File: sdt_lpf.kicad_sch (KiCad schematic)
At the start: 54 parts, among them J1 5-1814832-1, J2 5-1814832-1, J3 Conn_02x05_Odd_Even, U1 MASWSS0179, U10 MASWSS0179, U11 74LVC14AS14-13, U2 MASWSS0179, U3 MASWSS0179, U4 MASWSS0179, U5 MASWSS0179, U6 MASWSS0179, U7 MASWSS0179, U8 MASWSS0179, U9 MASWSS0179

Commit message: Commit before SSD update.
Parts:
- C1: footprint (none) -> 74LVC14:SO14_DIO
- C10, C11, C12, C13, C14, C15, C16, C17, C18, C19, C2, C20, C21, C22, C23, C24, C25, C3, C4, C5, C6, C7, C8, C9: footprint (none) -> Capacitor_SMD:C_1206_3216Metric
- R1: footprint (none) -> Resistor_SMD:R_1206_3216Metric
- U11: footprint SO14_DIO -> 74LVC14:SO14_DIO
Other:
- note added: "0.32 uH"
- note added: "0.4 uH"
- note added: "0.58u"
- note added: "1 db ripple Chebyshev 5th order coefficients 2.1349 1.0911 3.0009 1.0911 2.1349"
- note added: "1.09 uH"
- note added: "1.74 uH"
- note added: "1195 pF"
- note added: "1360 pF"
- note added: "15 MHz cut-off"
- note added: "1911 pF"
- note added: "22 MHz cut-off"
- note added: "227 pF"
- note added: "30 MHz cut-off"
- note added: "309 pF"
- note added: "319 pF"
- note added: "434 pF"
- note added: "453p"
- note added: "5 MHz cut-off"
- note added: "637p"
- note added: "8 MHz cut-off"
- note added: "850 pF"
- moved on the sheet: C1, C10, C11, C12, C13, C14, C15, C16, C17, C18, C19, C2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

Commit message: Released to PCBWay June 23.
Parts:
- removed D1, D2, D3, D4: 1N4148W, Diode_SMD:D_SOD-123, symbol Diode:1N4148W
- removed R1: R_US, Resistor_SMD:R_1206_3216Metric, symbol Device:R_US
- removed U11: 74LVC14AS14-13, 74LVC14:SO14_DIO, symbol 74LVC14AS14-13:74LVC14AS14-13
- added C26, C27, C28, C29, C30: 0.01u, Capacitor_SMD:C_1206_3216Metric, symbol Device:C
- added C31, C32, C33, C34, C35, C36: 0.1u, Capacitor_SMD:C_1206_3216Metric, symbol Device:C
- added H1, H2, H3, H4: MountingHole, MountingHole:MountingHole_3.2mm_M3, symbol Mechanical:MountingHole
- added J3: 22-23-2021, digikey-footprints:PinHeader_1x2_P2.54mm_Drill1.02mm, symbol dk_Rectangular-Connectors-Headers-Male-Pins:22-23-2021
- added U12: SN74HCS21, 74LVC14:SO14_DIO, symbol dk_Logic-Buffers-Drivers-Receivers-Transceivers:SN74HCS21
- C1: renamed from C16; value C -> 0.01u
- C2: renamed from C17; value C -> 0.01u
- C21: renamed from C25; value C -> 0.01u
- C22: renamed from C24; value C -> 0.01u
- C23: value C -> 0.01u
- C24: renamed from C22; value C -> 0.01u
- C25: renamed from C21; value C -> 0.01u
- C3: renamed from C18; value C -> 0.01u
- C4: renamed from C19; value C -> 0.01u
- C5: renamed from C20; value C -> 0.01u
- C7: renamed from C1; footprint 74LVC14:SO14_DIO -> Capacitor_SMD:C_1206_3216Metric
- J4: renamed from J3; footprint (none) -> Connector_PinHeader_2.54mm:PinHeader_2x05_P2.54mm_Vertical
- L1: renamed from L9; footprint (none) -> Toroid_SMD:Toroid_SMD
- L10: renamed from L8; footprint (none) -> Toroid_SMD:Toroid_SMD
- L2: renamed from L1; footprint (none) -> Toroid_SMD:Toroid_SMD
- L3: footprint (none) -> Toroid_SMD:Toroid_SMD
- L4: renamed from L5; footprint (none) -> Toroid_SMD:Toroid_SMD
- L5: renamed from L6; footprint (none) -> Toroid_SMD:Toroid_SMD
- L6: renamed from L10; footprint (none) -> Toroid_SMD:Toroid_SMD
- L7: renamed from L2; footprint (none) -> Toroid_SMD:Toroid_SMD
- L8: renamed from L4; footprint (none) -> Toroid_SMD:Toroid_SMD
- L9: renamed from L7; footprint (none) -> Toroid_SMD:Toroid_SMD
- renumbered C8 to C10, C14 to C11, C2 to C12, C5 to C13, C9 to C14, C10 to C15, C15 to C16, C3 to C17, C6 to C18, C11 to C19, C12 to C20, C13 to C6, C4 to C8, C7 to C9, J2 to J1, J1 to J2, U9 to U1, U8 to U10, U5 to U4, U6 to U5, U10 to U6, U1 to U7, U4 to U8, U7 to U9
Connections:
- net 80M_INV is gone; now on net 80M_ON: U10.6 (V1), U5.6 (V1)
- net 10M_ON: now also U12.6 (1Y)
- net 15M_ON: now also C34.2, U12.5 (1D)
- net 20M_ON: now also C33.2, U12.4 (1C)
- net 3_3V: now also C36.2, U12.14 (VCC)
- net 40M_ON: now also U9.6 (V1), C32.2, U12.2 (1B)
- net 80M_ON: now also C31.2, U12.1 (1A); no longer U10.4 (V2), U5.4 (V2)
- net GND: now also U7.2 (GND), C31.1, C32.1, C33.1, C34.1, C35.1, C36.1, J3.2, U12.10 (2B), U12.12 (2C), U12.13 (2D), U12.7 (GND), U12.9 (2A)
- net at C20.1, L10.2: now also C30.1; no longer U10.5 (RFC)
- net RXTX: now reaches J4.10 (Pin_10)
- net RXTX: now also C35.2, J3.1
- net at C18.1, L8.2: now also C28.1; no longer U8.5 (RFC)
- net at C17.1, L7.2: now also C27.1; no longer U7.5 (RFC)
- net at C19.1, L9.2: now also C29.1; no longer U9.5 (RFC)
- net at C16.1, L6.2: now also C26.1; no longer U6.5 (RFC)
- net 40M_INV_OUT: now reaches U9.4 (V2)
- net 10M_INV renamed 10M_INV_IN
- net 10M_INV_IN: no longer U6.4 (V2)
- net 15M_INV renamed 15M_INV_IN
- net 15M_INV_IN: no longer U7.4 (V2)
- net 20M_INV renamed 20M_INV_IN
- net 20M_INV_IN: no longer U8.4 (V2)
- net 40M_INV renamed 40M_INV_IN
- new net: C28.2, U8.5 (RFC)
- new net: C30.2, U10.5 (RFC)
- new net: C26.2, U6.5 (RFC)
- new net: C27.2, U7.5 (RFC)
- new net: C29.2, U9.5 (RFC)
- new net 10M_INV_OUT: U6.4 (V2)
- new net 15M_INV_OUT: U7.4 (V2)
- new net 20M_INV_OUT: U8.4 (V2)
- new net 80M_INV_IN: U5.4 (V2)
- new net 80M_INV_OUT: U10.4 (V2)
- no-connect marks 0 -> 14
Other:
- added sheet Inverters (inverters.kicad_sch)
- note added: "The AND gate array is responsible for controlling the 10M filter. When 80, 40, 20, and 15 are low, the 10M filter is turned on."
- moved on the sheet: J4

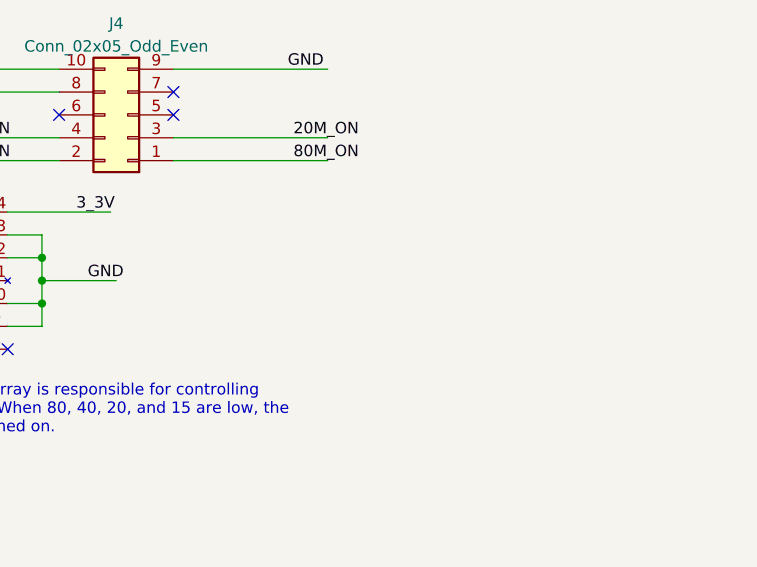
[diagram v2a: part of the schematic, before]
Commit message: Clean-up after first prototype build.
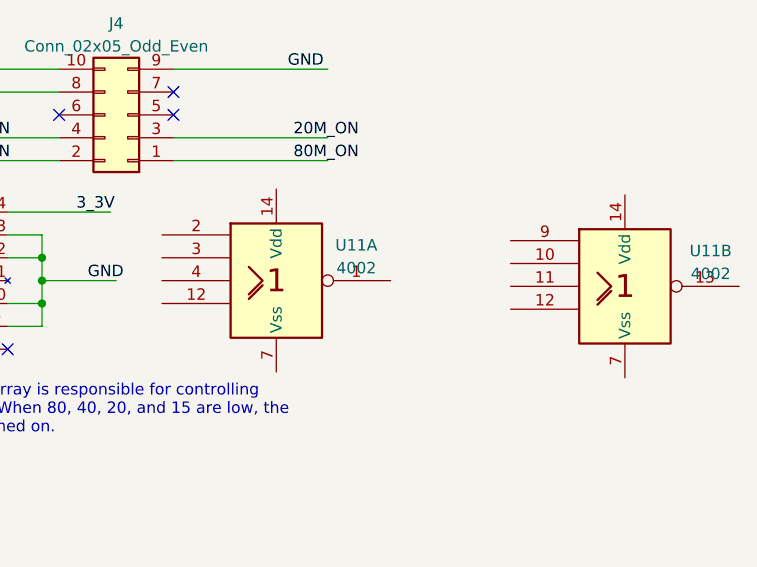
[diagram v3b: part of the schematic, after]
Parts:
- added U11: 4002, symbol 4xxx_IEEE:4002
- J4: footprint Connector_PinHeader_2.54mm:PinHeader_2x05_P2.54mm_Vertical -> Connector_IDC:IDC-Header_2x05_P2.54mm_Vertical
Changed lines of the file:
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@@
       (effects (font (size 1.27 1.27)))
     )
-    (property "Footprint" "Connector_PinHeader_2.54mm:PinHeader_2x05_P2.54mm_Vertical" (at 237.49 135.255 0)
+    (property "Footprint" "Connector_IDC:IDC-Header_2x05_P2.54mm_Vertical" (at 237.49 135.255 0)
       (effects (font (size 1.27 1.27)) hide)
     )
@@
     )
   )
+  (symbol (lib_id "4xxx_IEEE:4002") (at 254 153.67 0) (unit 1)
+    (in_bom yes) (on_board yes) (dnp no) (fields_autoplaced)
+    (property "Reference" "U11" (at 262.89 149.7331 0)
+      (effects (font (size 1.27 1.27)))
+    )
+    (property "Value" "4002" (at 262.89 152.2731 0)
+      (effects (font (size 1.27 1.27)))
+    )
+    (property "Footprint" "" (at 254 153.67 0)
+      (effects (font (size 1.27 1.27)) hide)
+    )
+    (property "Datasheet" "" (at 254 153.67 0)
+      (effects (font (size 1.27 1.27)) hide)
+    )
+    (pin "14")
+    (pin "7")
+    (pin "1")
+    (pin "12")
+    (pin "2")
+    (pin "3")
+    (pin "4")
+    (pin "10")
+    (pin "11")
+    (pin "12")
+    (pin "13")
+    (pin "9")
+    (instances
+      (project "sdt_lpf"
+        (path "/528f45ff-5641-4aeb-93d2-897e9e2c12f9"
+          (reference "U11") (unit 1)
+        )
+      )
+    )
+  )
   (symbol (lib_id "Device:L") (at 116.205 67.945 90) (unit 1)
     (in_bom yes) (on_board yes) (dnp no) (fields_autoplaced)
@@
         )
       )
+    )
+  )
+  (symbol (lib_id "4xxx_IEEE:4002") (at 292.735 154.305 0) (unit 2)
+    (in_bom yes) (on_board yes) (dnp no) (fields_autoplaced)
+    (property "Reference" "U11" (at 302.26 150.3681 0)
+      (effects (font (size 1.27 1.27)))
+    )
+    (property "Value" "4002" (at 302.26 152.9081 0)
+      (effects (font (size 1.27 1.27)))
+    )
+    (property "Footprint" "" (at 292.735 154.305 0)
+      (effects (font (size 1.27 1.27)) hide)
+    )
+    (property "Datasheet" "" (at 292.735 154.305 0)
+      (effects (font (size 1.27 1.27)) hide)
+    )
+    (pin "14")
+    (pin "7")
+    (pin "1")
+    (pin "12")
+    (pin "2")
+    (pin "3")
+    (pin "4")
+    (pin "10")
+    (pin "11")
+    (pin "12")
+    (pin "13")
+    (pin "9")
+    (instances
+      (project "sdt_lpf"
+        (path "/528f45ff-5641-4aeb-93d2-897e9e2c12f9"
+          (reference "U11") (unit 2)
+        )
+      )

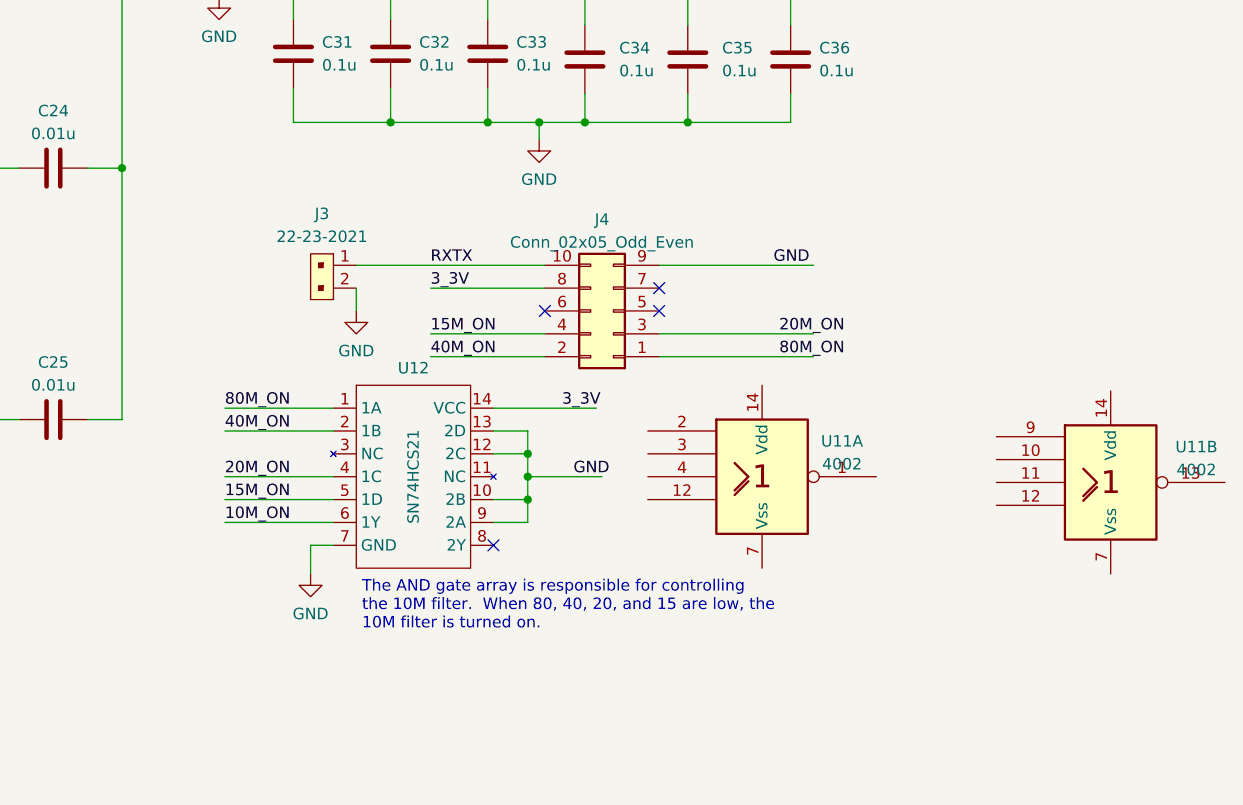
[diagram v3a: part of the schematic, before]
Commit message: Fixed logic gate, is now NOR.  Cleaned up layout.
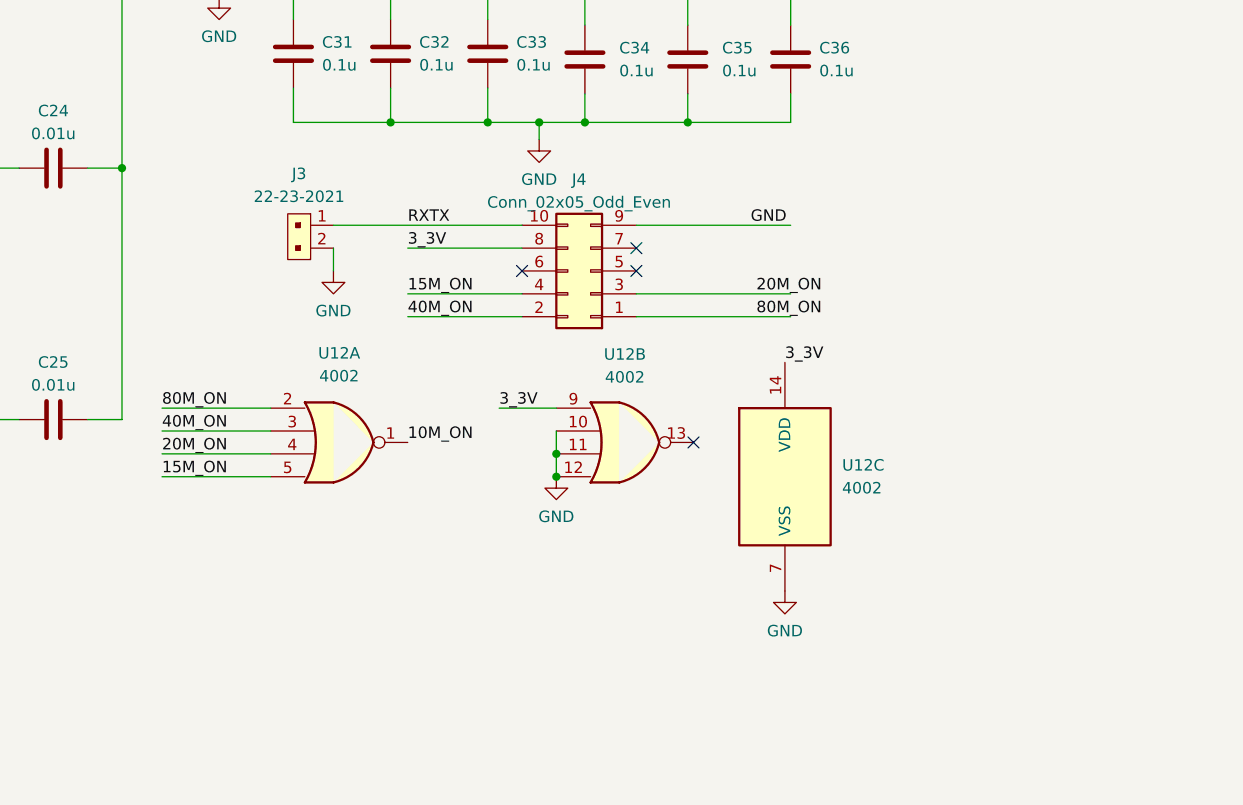
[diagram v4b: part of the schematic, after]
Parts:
- removed U11: 4002, symbol 4xxx_IEEE:4002
- removed U12: SN74HCS21, 74LVC14:SO14_DIO, symbol dk_Logic-Buffers-Drivers-Receivers-Transceivers:SN74HCS21
- added U12: 4002, Package_SO:SOIC-14_3.9x8.7mm_P1.27mm, symbol 4xxx:4002
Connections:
- net 10M_ON: now also U12.1
- net 15M_ON: now also U12.5
- net 20M_ON: now also U12.4
- net 3_3V: now also U12.14 (VDD), U12.9
- net 40M_ON: now also U12.3
- net 80M_ON: now also U12.2
- net GND: now also U12.10, U12.11, U12.12, U12.7 (VSS)
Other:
- note removed: "The AND gate array is responsible for controlling the 10M filter. When 80, 40, 20, and 15 are low, the 10M filter is turned on."
- moved on the sheet: J3, J4
